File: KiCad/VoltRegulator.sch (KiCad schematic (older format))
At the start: 3 parts

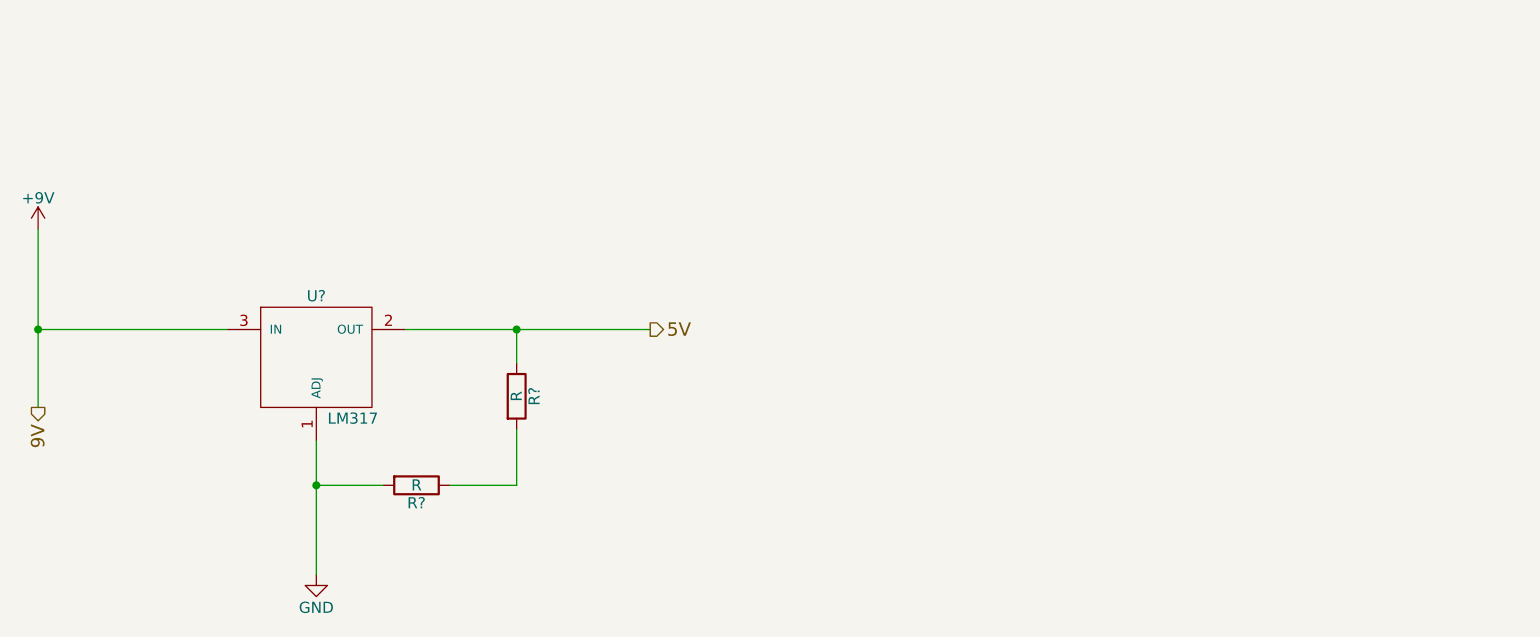
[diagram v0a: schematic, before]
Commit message: Added the Hbridge
The schematics is almost completed with all the values set on resitors
and all the components should be there. Minor changes is to be expected
though.
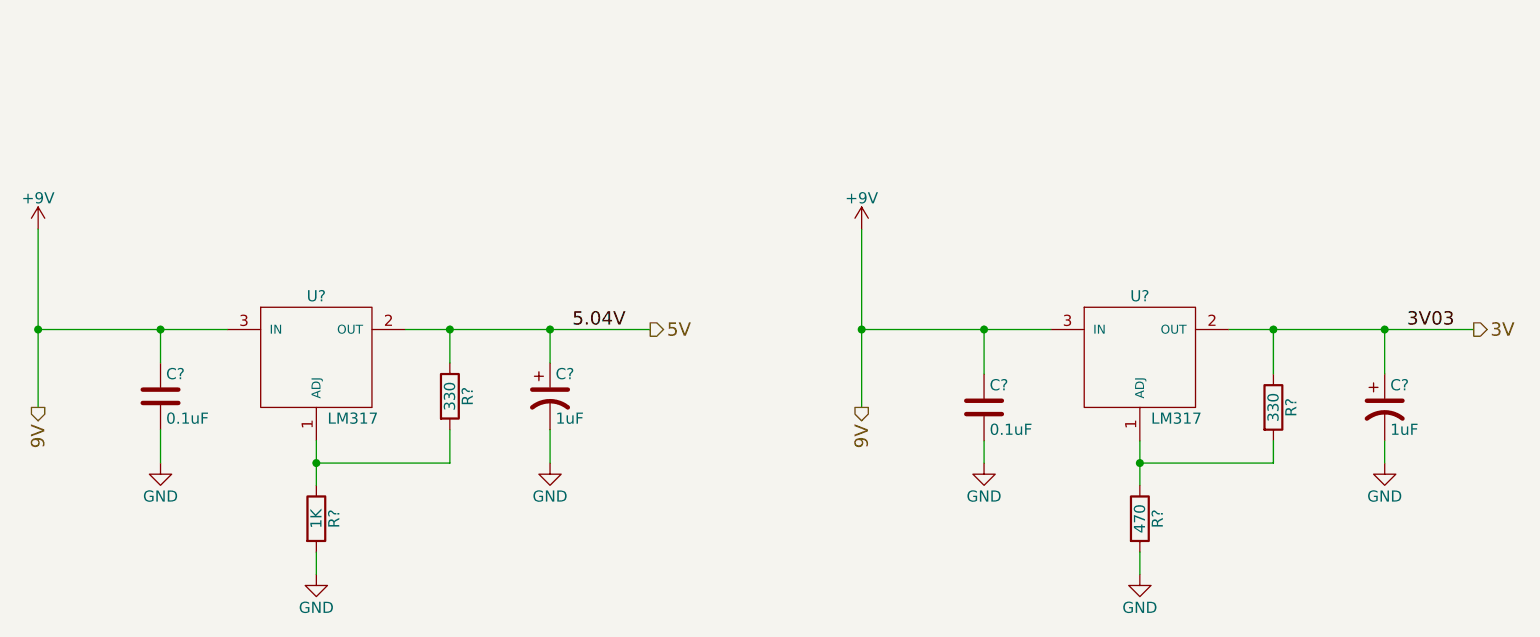
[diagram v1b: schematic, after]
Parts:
- added C? (x2): 1uF, symbol CP1
- added C? (x2): 0.1uF, symbol C
- added R?: 330, symbol R
- added R?: 470, symbol R
- added U?: LM317, symbol LM317_SOT223
- R?: value R -> 330
- R?: value R -> 1K
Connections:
- net +9V: now also C?.1, C?.1, U?.3 (IN)
- net 5V: now also C?.1
- net GND: now also C?.2, C?.2, C?.2, C?.2, R?.2; no longer U?.1 (ADJ)
- net at R?.1, R?.2: now also U?.1 (ADJ)
- new net: R?.1, R?.2, U?.1 (ADJ)
- new net 3V: C?.1, R?.1, U?.2 (OUT)
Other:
- moved on the sheet: R?
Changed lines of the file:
@@
 LIBS:valves
 LIBS:ir_recieve
+LIBS:I2C_LCD
+LIBS:LinkuraModule
+LIBS:i2cdisplay
+LIBS:ca3240e
+LIBS:SN754410NE
+LIBS:motor
 LIBS:Project-cache
 EELAYER 25 0
@@
 $Descr A4 11693 8268
 encoding utf-8
-Sheet 2 4
+Sheet 2 7
 Title ""
 Date ""
@@
 L R R?
 U 1 1 57161132
-P 4950 2750
-F 0 "R?" V 5030 2750 50  0000 C CNN
-F 1 "R" V 4950 2750 50  0000 C CNN
-F 2 "" V 4880 2750 50  0000 C CNN
-F 3 "" H 4950 2750 50  0000 C CNN
-	1    4950 2750
+P 4650 2750
+F 0 "R?" V 4730 2750 50  0000 C CNN
+F 1 "330" V 4650 2750 50  0000 C CNN
+F 2 "" V 4580 2750 50  0000 C CNN
+F 3 "" H 4650 2750 50  0000 C CNN
+	1    4650 2750
 	1    0    0    -1
 $EndComp
@@
 L R R?
 U 1 1 5716119D
-P 4500 3150
-F 0 "R?" V 4580 3150 50  0000 C CNN
-F 1 "R" V 4500 3150 50  0000 C CNN
-F 2 "" V 4430 3150 50  0000 C CNN
-F 3 "" H 4500 3150 50  0000 C CNN
-	1    4500 3150
-	0    1    1    0
-$EndComp
-Wire Wire Line
-	4050 2950 4050 3550
-Wire Wire Line
-	4350 3150 4050 3150
-Connection ~ 4050 3150
-Wire Wire Line
-	4650 3150 4950 3150
-Wire Wire Line
-	4950 3150 4950 2900
-Wire Wire Line
-	4950 2600 4950 2450
+P 4050 3300
+F 0 "R?" V 4130 3300 50  0000 C CNN
+F 1 "1K" V 4050 3300 50  0000 C CNN
+F 2 "" V 3980 3300 50  0000 C CNN
+F 3 "" H 4050 3300 50  0000 C CNN
+	1    4050 3300
+	1    0    0    -1
+$EndComp
 Wire Wire Line
 	4450 2450 5550 2450
@@
 Text HLabel 5550 2450 2    60   Output ~ 0
 5V
-Connection ~ 4950 2450
 $Comp
 L GND #PWR?
@@
 	1    0    0    -1
 $EndComp
+$Comp
+L LM317_SOT223 U?
+U 1 1 571810AE
+P 7750 2600
+F 0 "U?" H 7750 2900 50  0000 C CNN
+F 1 "LM317" H 7800 2350 50  0000 L CNN
+F 2 "" H 7750 2600 50  0000 C CNN
+F 3 "" H 7750 2600 50  0000 C CNN
+	1    7750 2600
+	1    0    0    -1
+$EndComp
+$Comp
+L +9V #PWR?
+U 1 1 571810B4
+P 6500 2000
+F 0 "#PWR?" H 6500 1850 50  0001 C CNN
+F 1 "+9V" H 6500 2140 50  0000 C CNN
+F 2 "" H 6500 2000 50  0000 C CNN
+F 3 "" H 6500 2000 50  0000 C CNN
+	1    6500 2000
+	1    0    0    -1
+$EndComp
+$Comp
+L R R?
+U 1 1 571810BA
+P 8350 2800
+F 0 "R?" V 8430 2800 50  0000 C CNN
+F 1 "330" V 8350 2800 50  0000 C CNN
+F 2 "" V 8280 2800 50  0000 C CNN
+F 3 "" H 8350 2800 50  0000 C CNN
+	1    8350 2800
+	1    0    0    -1
+$EndComp
+$Comp
+L R R?
+U 1 1 571810C0
+P 7750 3300
+F 0 "R?" V 7830 3300 50  0000 C CNN
+F 1 "470" V 7750 3300 50  0000 C CNN
+F 2 "" V 7680 3300 50  0000 C CNN
+F 3 "" H 7750 3300 50  0000 C CNN
+	1    7750 3300
+	1    0    0    -1
+$EndComp
+Wire Wire Line
+	8150 2450 9250 2450
+Wire Wire Line
+	6500 2000 6500 2800
+Wire Wire Line
+	6500 2450 7350 2450
+Connection ~ 6500 2450
+Text HLabel 6500 2800 3    60   Output ~ 0
+9V
+Text HLabel 9250 2450 2    60   Output ~ 0
+3V
+$Comp
+L GND #PWR?
+U 1 1 571810D3
+P 7750 3550
+F 0 "#PWR?" H 7750 3300 50  0001 C CNN
+F 1 "GND" H 7750 3400 50  0000 C CNN
+F 2 "" H 7750 3550 50  0000 C CNN
+F 3 "" H 7750 3550 50  0000 C CNN
+	1    7750 3550
+	1    0    0    -1
+$EndComp
+Text Label 5200 2450 0    60   ~ 0
+5.04V
+Text Label 8950 2450 0    60   ~ 0
+3V03
+Wire Wire Line
+	8350 2450 8350 2650
+Connection ~ 8350 2450
+Wire Wire Line
+	8350 2950 8350 3050
+Wire Wire Line
+	8350 3050 7750 3050
+Wire Wire Line
+	7750 2950 7750 3150
+Connection ~ 7750 3050
+Wire Wire Line
+	7750 3450 7750 3550
+Wire Wire Line
+	4650 2450 4650 2600
+Connection ~ 4650 2450
+Wire Wire Line
+	4650 2900 4650 3050
+Wire Wire Line
+	4650 3050 4050 3050
+Wire Wire Line
+	4050 2950 4050 3150
+Connection ~ 4050 3050
+Wire Wire Line
+	4050 3450 4050 3550
+$Comp
+L CP1 C?
+U 1 1 571BB487
+P 5100 2750
+F 0 "C?" H 5125 2850 50  0000 L CNN
+F 1 "1uF" H 5125 2650 50  0000 L CNN
+F 2 "" H 5100 2750 50  0000 C CNN
+F 3 "" H 5100 2750 50  0000 C CNN
+	1    5100 2750
+	1    0    0    -1
+$EndComp
+$Comp
+L CP1 C?
+U 1 1 571BB503
+P 8850 2800
+F 0 "C?" H 8875 2900 50  0000 L CNN
+F 1 "1uF" H 8875 2700 50  0000 L CNN
+F 2 "" H 8850 2800 50  0000 C CNN
+F 3 "" H 8850 2800 50  0000 C CNN
+	1    8850 2800
+	1    0    0    -1
+$EndComp
+Wire Wire Line
+	8850 2650 8850 2450
+Connection ~ 8850 2450
+Wire Wire Line
+	5100 2600 5100 2450
+Connection ~ 5100 2450
+Wire Wire Line
+	5100 2900 5100 3050
+Wire Wire Line
+	8850 2950 8850 3050
+$Comp
+L C C?
+U 1 1 571BBB0A
+P 3350 2750
+F 0 "C?" H 3375 2850 50  0000 L CNN
+F 1 "0.1uF" H 3375 2650 50  0000 L CNN
+F 2 "" H 3388 2600 50  0000 C CNN
+F 3 "" H 3350 2750 50  0000 C CNN
+	1    3350 2750
+	1    0    0    -1
+$EndComp
+$Comp
+L C C?
+U 1 1 571BBC58
+P 7050 2800
+F 0 "C?" H 7075 2900 50  0000 L CNN
+F 1 "0.1uF" H 7075 2700 50  0000 L CNN
+F 2 "" H 7088 2650 50  0000 C CNN
+F 3 "" H 7050 2800 50  0000 C CNN
+	1    7050 2800
+	1    0    0    -1
+$EndComp
+Wire Wire Line
+	7050 2450 7050 2650
+Connection ~ 7050 2450
+Wire Wire Line
+	7050 2950 7050 3050
+Wire Wire Line
+	3350 2600 3350 2450
+Connection ~ 3350 2450
+Wire Wire Line
+	3350 2900 3350 3050
+$Comp
+L GND #PWR?
+U 1 1 571BC1AC
+P 3350 3050
+F 0 "#PWR?" H 3350 2800 50  0001 C CNN
+F 1 "GND" H 3350 2900 50  0000 C CNN
+F 2 "" H 3350 3050 50  0000 C CNN
+F 3 "" H 3350 3050 50  0000 C CNN
+	1    3350 3050
+	1    0    0    -1
+$EndComp
+$Comp
+L GND #PWR?
+U 1 1 571BC2DA
+P 5100 3050
+F 0 "#PWR?" H 5100 2800 50  0001 C CNN
+F 1 "GND" H 5100 2900 50  0000 C CNN
+F 2 "" H 5100 3050 50  0000 C CNN
+F 3 "" H 5100 3050 50  0000 C CNN
+	1    5100 3050
+	1    0    0    -1
+$EndComp
+$Comp
+L GND #PWR?
+U 1 1 571BC41B
+P 7050 3050
+F 0 "#PWR?" H 7050 2800 50  0001 C CNN
+F 1 "GND" H 7050 2900 50  0000 C CNN
+F 2 "" H 7050 3050 50  0000 C CNN
+F 3 "" H 7050 3050 50  0000 C CNN
+	1    7050 3050
+	1    0    0    -1
+$EndComp
+$Comp
+L GND #PWR?
+U 1 1 571BC444
+P 8850 3050
+F 0 "#PWR?" H 8850 2800 50  0001 C CNN
+F 1 "GND" H 8850 2900 50  0000 C CNN
+F 2 "" H 8850 3050 50  0000 C CNN
+F 3 "" H 8850 3050 50  0000 C CNN
+	1    8850 3050
+	1    0    0    -1
+$EndComp

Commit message: Updated the schematics and started with the PCB
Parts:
- C3, C5: renamed from C?; footprint (none) -> Capacitors_ThroughHole:C_Disc_D3_P2.5
- C4, C6: renamed from C?; footprint (none) -> Capacitors_ThroughHole:C_Radial_D5_L6_P2.5
- R22, R5, R6, R7: renamed from R?; footprint (none) -> Resistors_ThroughHole:Resistor_Vertical_RM5mm
- U2, U3: renamed from U?; footprint (none) -> TO_SOT_Packages_THT:TO-220_Neutral123_Vertical
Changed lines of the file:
@@
 $Descr A4 11693 8268
 encoding utf-8
-Sheet 2 7
+Sheet 2 6
 Title ""
 Date ""
@@
 $EndDescr
 $Comp
-L LM317_SOT223 U?
+L LM317_SOT223 U2
 U 1 1 57160D0E
 P 4050 2600
-F 0 "U?" H 4050 2900 50  0000 C CNN
+F 0 "U2" H 4050 2900 50  0000 C CNN
 F 1 "LM317" H 4100 2350 50  0000 L CNN
-F 2 "" H 4050 2600 50  0000 C CNN
+F 2 "TO_SOT_Packages_THT:TO-220_Neutral123_Vertical" H 4050 2600 50  0001 C CNN
 F 3 "" H 4050 2600 50  0000 C CNN
 	1    4050 2600
@@
 $EndComp
 $Comp
-L +9V #PWR?
+L +9V #PWR08
 U 1 1 571610CA
 P 2800 2000
-F 0 "#PWR?" H 2800 1850 50  0001 C CNN
+F 0 "#PWR08" H 2800 1850 50  0001 C CNN
 F 1 "+9V" H 2800 2140 50  0000 C CNN
 F 2 "" H 2800 2000 50  0000 C CNN
@@
 $EndComp
 $Comp
-L R R?
+L R R6
 U 1 1 57161132
 P 4650 2750
-F 0 "R?" V 4730 2750 50  0000 C CNN
+F 0 "R6" V 4730 2750 50  0000 C CNN
 F 1 "330" V 4650 2750 50  0000 C CNN
-F 2 "" V 4580 2750 50  0000 C CNN
+F 2 "Resistors_ThroughHole:Resistor_Vertical_RM5mm" V 4580 2750 50  0001 C CNN
 F 3 "" H 4650 2750 50  0000 C CNN
 	1    4650 2750
@@
 $EndComp
 $Comp
-L R R?
+L R R5
 U 1 1 5716119D
 P 4050 3300
-F 0 "R?" V 4130 3300 50  0000 C CNN
+F 0 "R5" V 4130 3300 50  0000 C CNN
 F 1 "1K" V 4050 3300 50  0000 C CNN
-F 2 "" V 3980 3300 50  0000 C CNN
+F 2 "Resistors_ThroughHole:Resistor_Vertical_RM5mm" V 3980 3300 50  0001 C CNN
 F 3 "" H 4050 3300 50  0000 C CNN
 	1    4050 3300
@@
 5V
 $Comp
-L GND #PWR?
+L GND #PWR09
 U 1 1 571613A6
 P 4050 3550
-F 0 "#PWR?" H 4050 3300 50  0001 C CNN
+F 0 "#PWR09" H 4050 3300 50  0001 C CNN
 F 1 "GND" H 4050 3400 50  0000 C CNN
 F 2 "" H 4050 3550 50  0000 C CNN
@@
 $EndComp
 $Comp
-L LM317_SOT223 U?
+L LM317_SOT223 U3
 U 1 1 571810AE
 P 7750 2600
-F 0 "U?" H 7750 2900 50  0000 C CNN
+F 0 "U3" H 7750 2900 50  0000 C CNN
 F 1 "LM317" H 7800 2350 50  0000 L CNN
-F 2 "" H 7750 2600 50  0000 C CNN
+F 2 "TO_SOT_Packages_THT:TO-220_Neutral123_Vertical" H 7750 2600 50  0001 C CNN
 F 3 "" H 7750 2600 50  0000 C CNN
 	1    7750 2600
@@
 $EndComp
 $Comp
-L +9V #PWR?
+L +9V #PWR010
 U 1 1 571810B4
 P 6500 2000
-F 0 "#PWR?" H 6500 1850 50  0001 C CNN
+F 0 "#PWR010" H 6500 1850 50  0001 C CNN
 F 1 "+9V" H 6500 2140 50  0000 C CNN
 F 2 "" H 6500 2000 50  0000 C CNN
@@
 $EndComp
 $Comp
-L R R?
+L R R22
 U 1 1 571810BA
 P 8350 2800
-F 0 "R?" V 8430 2800 50  0000 C CNN
+F 0 "R22" V 8430 2800 50  0000 C CNN
 F 1 "330" V 8350 2800 50  0000 C CNN
-F 2 "" V 8280 2800 50  0000 C CNN
+F 2 "Resistors_ThroughHole:Resistor_Vertical_RM5mm" V 8280 2800 50  0001 C CNN
 F 3 "" H 8350 2800 50  0000 C CNN
 	1    8350 2800
@@
 $EndComp
 $Comp
-L R R?
+L R R7
 U 1 1 571810C0
 P 7750 3300
-F 0 "R?" V 7830 3300 50  0000 C CNN
+F 0 "R7" V 7830 3300 50  0000 C CNN
 F 1 "470" V 7750 3300 50  0000 C CNN
-F 2 "" V 7680 3300 50  0000 C CNN
+F 2 "Resistors_ThroughHole:Resistor_Vertical_RM5mm" V 7680 3300 50  0001 C CNN
 F 3 "" H 7750 3300 50  0000 C CNN
 	1    7750 3300
@@
 3V
 $Comp
-L GND #PWR?
+L GND #PWR011
 U 1 1 571810D3
 P 7750 3550
-F 0 "#PWR?" H 7750 3300 50  0001 C CNN
+F 0 "#PWR011" H 7750 3300 50  0001 C CNN
 F 1 "GND" H 7750 3400 50  0000 C CNN
 F 2 "" H 7750 3550 50  0000 C CNN
@@
 	4050 3450 4050 3550
 $Comp
-L CP1 C?
+L CP1 C4
 U 1 1 571BB487
 P 5100 2750
-F 0 "C?" H 5125 2850 50  0000 L CNN
+F 0 "C4" H 5125 2850 50  0000 L CNN
 F 1 "1uF" H 5125 2650 50  0000 L CNN
-F 2 "" H 5100 2750 50  0000 C CNN
+F 2 "Capacitors_ThroughHole:C_Radial_D5_L6_P2.5" H 5100 2750 50  0001 C CNN
 F 3 "" H 5100 2750 50  0000 C CNN
 	1    5100 2750
@@
 $EndComp
 $Comp
-L CP1 C?
+L CP1 C6
 U 1 1 571BB503
 P 8850 2800
-F 0 "C?" H 8875 2900 50  0000 L CNN
+F 0 "C6" H 8875 2900 50  0000 L CNN
 F 1 "1uF" H 8875 2700 50  0000 L CNN
-F 2 "" H 8850 2800 50  0000 C CNN
+F 2 "Capacitors_ThroughHole:C_Radial_D5_L6_P2.5" H 8850 2800 50  0001 C CNN
 F 3 "" H 8850 2800 50  0000 C CNN
 	1    8850 2800
@@
 	8850 2950 8850 3050
 $Comp
-L C C?
+L C C3
 U 1 1 571BBB0A
 P 3350 2750
-F 0 "C?" H 3375 2850 50  0000 L CNN
+F 0 "C3" H 3375 2850 50  0000 L CNN
 F 1 "0.1uF" H 3375 2650 50  0000 L CNN
-F 2 "" H 3388 2600 50  0000 C CNN
+F 2 "Capacitors_ThroughHole:C_Disc_D3_P2.5" H 3388 2600 50  0001 C CNN
 F 3 "" H 3350 2750 50  0000 C CNN
 	1    3350 2750
@@
 $EndComp
 $Comp
-L C C?
+L C C5
 U 1 1 571BBC58
 P 7050 2800
-F 0 "C?" H 7075 2900 50  0000 L CNN
+F 0 "C5" H 7075 2900 50  0000 L CNN
 F 1 "0.1uF" H 7075 2700 50  0000 L CNN
-F 2 "" H 7088 2650 50  0000 C CNN
+F 2 "Capacitors_ThroughHole:C_Disc_D3_P2.5" H 7088 2650 50  0001 C CNN
 F 3 "" H 7050 2800 50  0000 C CNN
 	1    7050 2800
@@
 	3350 2900 3350 3050
 $Comp
-L GND #PWR?
+L GND #PWR012
 U 1 1 571BC1AC
 P 3350 3050
-F 0 "#PWR?" H 3350 2800 50  0001 C CNN
+F 0 "#PWR012" H 3350 2800 50  0001 C CNN
 F 1 "GND" H 3350 2900 50  0000 C CNN
 F 2 "" H 3350 3050 50  0000 C CNN
@@
 $EndComp
 $Comp
-L GND #PWR?
+L GND #PWR013
 U 1 1 571BC2DA
 P 5100 3050
-F 0 "#PWR?" H 5100 2800 50  0001 C CNN
+F 0 "#PWR013" H 5100 2800 50  0001 C CNN
 F 1 "GND" H 5100 2900 50  0000 C CNN
 F 2 "" H 5100 3050 50  0000 C CNN
@@
 $EndComp
 $Comp
-L GND #PWR?
+L GND #PWR014
 U 1 1 571BC41B
 P 7050 3050
-F 0 "#PWR?" H 7050 2800 50  0001 C CNN
+F 0 "#PWR014" H 7050 2800 50  0001 C CNN
 F 1 "GND" H 7050 2900 50  0000 C CNN
 F 2 "" H 7050 3050 50  0000 C CNN
@@
 $EndComp
 $Comp
-L GND #PWR?
+L GND #PWR015
 U 1 1 571BC444
 P 8850 3050
-F 0 "#PWR?" H 8850 2800 50  0001 C CNN
+F 0 "#PWR015" H 8850 2800 50  0001 C CNN
 F 1 "GND" H 8850 2900 50  0000 C CNN
 F 2 "" H 8850 3050 50  0000 C CNN

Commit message: Started to do the routing
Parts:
- added P7: CONN_01X02, Pin_Headers:Pin_Header_Straight_1x02, symbol CONN_01X02
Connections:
- net GND: now also P7.2 (P2)
- net +9V renamed 9V
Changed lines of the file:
@@
-$EndComp
-$Comp
-L +9V #PWR08
-U 1 1 571610CA
-P 2800 2000
-F 0 "#PWR08" H 2800 1850 50  0001 C CNN
-F 1 "+9V" H 2800 2140 50  0000 C CNN
-F 2 "" H 2800 2000 50  0000 C CNN
-F 3 "" H 2800 2000 50  0000 C CNN
-	1    2800 2000
-	1    0    0    -1
 $EndComp
 $Comp
@@
 5V
 $Comp
-L GND #PWR09
+L GND #PWR9
 U 1 1 571613A6
 P 4050 3550
-F 0 "#PWR09" H 4050 3300 50  0001 C CNN
+F 0 "#PWR9" H 4050 3300 50  0001 C CNN
 F 1 "GND" H 4050 3400 50  0000 C CNN
 F 2 "" H 4050 3550 50  0000 C CNN
@@
 $EndComp
 $Comp
-L +9V #PWR010
-U 1 1 571810B4
-P 6500 2000
-F 0 "#PWR010" H 6500 1850 50  0001 C CNN
-F 1 "+9V" H 6500 2140 50  0000 C CNN
-F 2 "" H 6500 2000 50  0000 C CNN
-F 3 "" H 6500 2000 50  0000 C CNN
-	1    6500 2000
-	1    0    0    -1
-$EndComp
-$Comp
 L R R22
 U 1 1 571810BA
@@
 3V
 $Comp
-L GND #PWR011
+L GND #PWR13
 U 1 1 571810D3
 P 7750 3550
-F 0 "#PWR011" H 7750 3300 50  0001 C CNN
+F 0 "#PWR13" H 7750 3300 50  0001 C CNN
 F 1 "GND" H 7750 3400 50  0000 C CNN
 F 2 "" H 7750 3550 50  0000 C CNN
@@
 	3350 2900 3350 3050
 $Comp
-L GND #PWR012
+L GND #PWR8
 U 1 1 571BC1AC
 P 3350 3050
-F 0 "#PWR012" H 3350 2800 50  0001 C CNN
+F 0 "#PWR8" H 3350 2800 50  0001 C CNN
 F 1 "GND" H 3350 2900 50  0000 C CNN
 F 2 "" H 3350 3050 50  0000 C CNN
@@
 $EndComp
 $Comp
-L GND #PWR013
+L GND #PWR11
 U 1 1 571BC2DA
 P 5100 3050
-F 0 "#PWR013" H 5100 2800 50  0001 C CNN
+F 0 "#PWR11" H 5100 2800 50  0001 C CNN
 F 1 "GND" H 5100 2900 50  0000 C CNN
 F 2 "" H 5100 3050 50  0000 C CNN
@@
 $EndComp
 $Comp
-L GND #PWR014
+L GND #PWR12
 U 1 1 571BC41B
 P 7050 3050
-F 0 "#PWR014" H 7050 2800 50  0001 C CNN
+F 0 "#PWR12" H 7050 2800 50  0001 C CNN
 F 1 "GND" H 7050 2900 50  0000 C CNN
 F 2 "" H 7050 3050 50  0000 C CNN
@@
 $EndComp
 $Comp
-L GND #PWR015
+L GND #PWR14
 U 1 1 571BC444
 P 8850 3050
-F 0 "#PWR015" H 8850 2800 50  0001 C CNN
+F 0 "#PWR14" H 8850 2800 50  0001 C CNN
 F 1 "GND" H 8850 2900 50  0000 C CNN
 F 2 "" H 8850 3050 50  0000 C CNN
@@
 	1    0    0    -1
 $EndComp
+$Comp
+L CONN_01X02 P7
+U 1 1 5735CB2D
+P 4750 1200
+F 0 "P7" H 4750 1350 50  0000 C CNN
+F 1 "CONN_01X02" V 4850 1200 50  0000 C CNN
+F 2 "Pin_Headers:Pin_Header_Straight_1x02" H 4750 1200 50  0001 C CNN
+F 3 "" H 4750 1200 50  0000 C CNN
+	1    4750 1200
+	0    -1   -1   0
+$EndComp
+Wire Wire Line
+	2800 2000 6500 2000
+Wire Wire Line
+	4700 1400 4700 2000
+Wire Wire Line
+	4800 1400 4800 1550
+Wire Wire Line
+	4800 1550 4900 1550
+$Comp
+L GND #PWR10
+U 1 1 5735CD07
+P 4900 1550
+F 0 "#PWR10" H 4900 1300 50  0001 C CNN
+F 1 "GND" H 4900 1400 50  0000 C CNN
+F 2 "" H 4900 1550 50  0000 C CNN
+F 3 "" H 4900 1550 50  0000 C CNN
+	1    4900 1550
+	0    -1   -1   0
+$EndComp
 $EndSCHEMATC
